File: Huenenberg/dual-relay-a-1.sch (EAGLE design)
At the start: 40 parts, among them J10 LARGE-SOLDERPAD, J11 LARGE-SOLDERPAD, J12 LARGE-SOLDERPAD, J13 LARGE-SOLDERPAD, J14 LARGE-SOLDERPAD, J15 LARGE-SOLDERPAD, J16 LARGE-SOLDERPAD, J17 LARGE-SOLDERPAD, J18 LARGE-SOLDERPAD, J19 LARGE-SOLDERPAD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

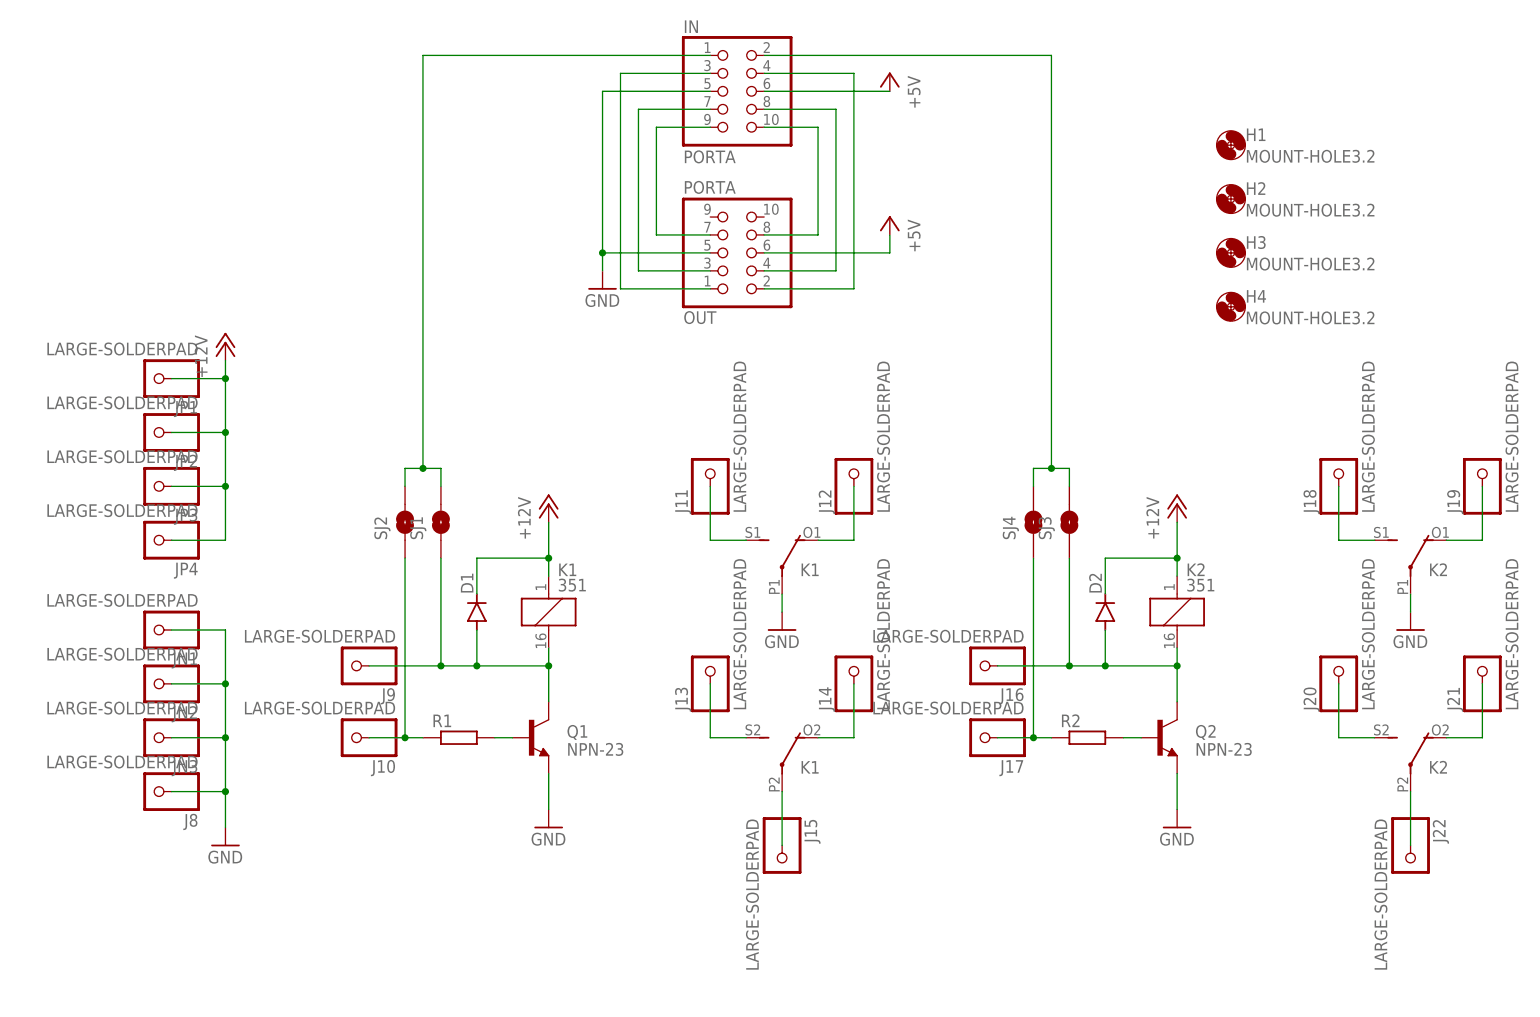
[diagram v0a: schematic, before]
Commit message: Adds values to the large solderpads that explain what should be connected.
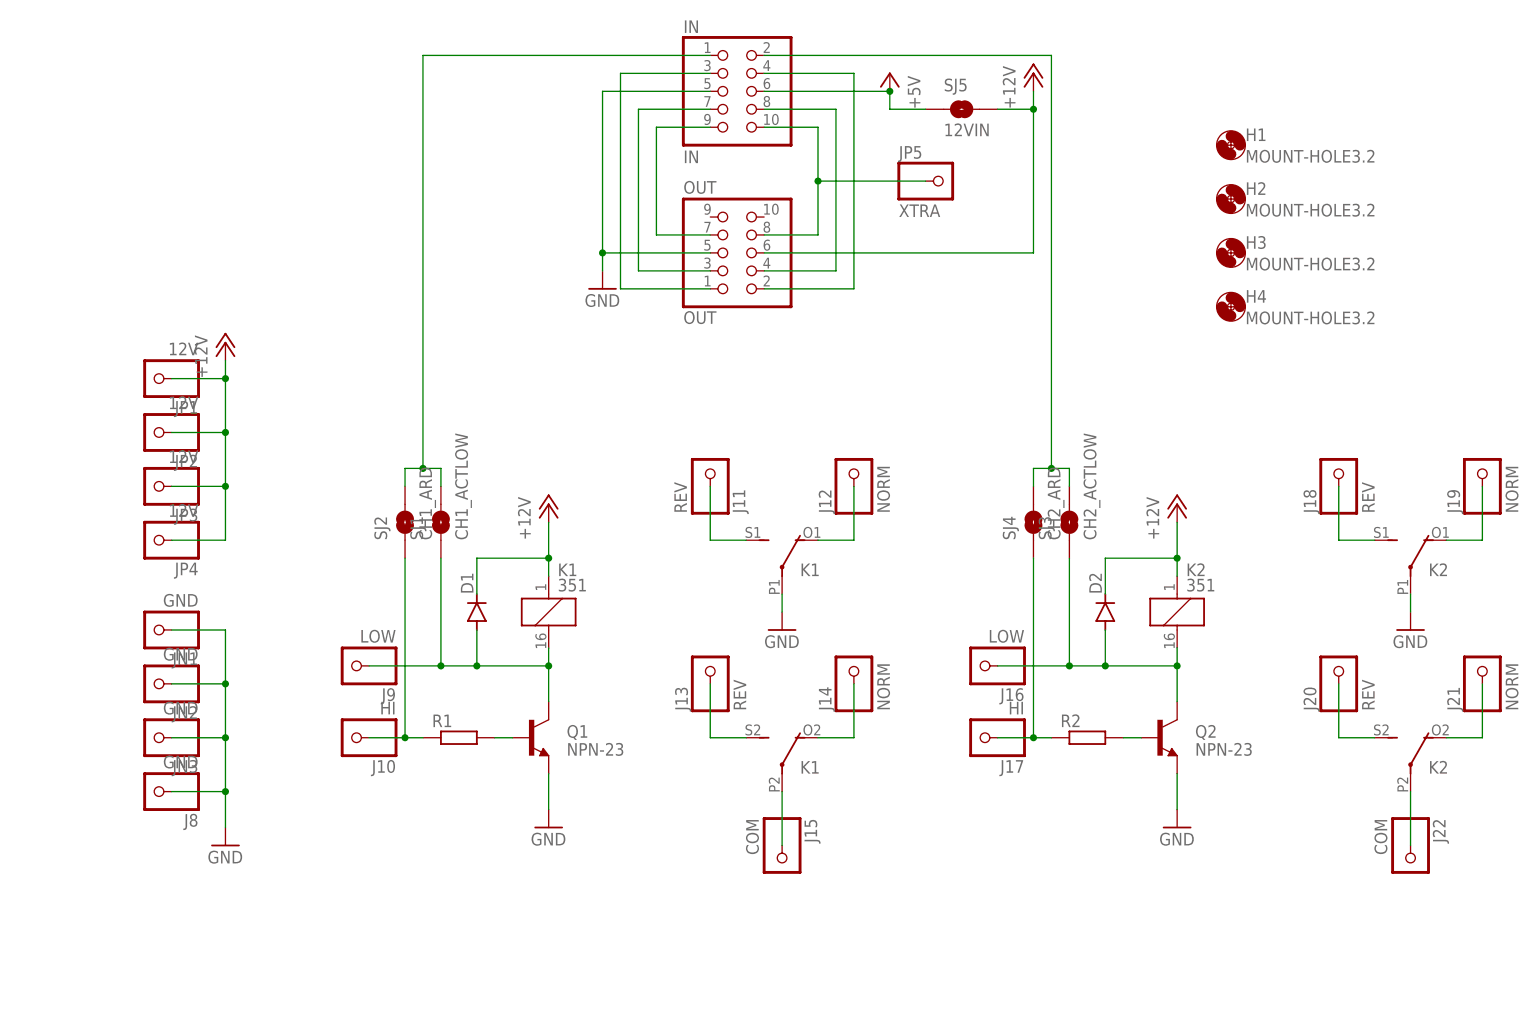
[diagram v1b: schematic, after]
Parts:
- added JP5: XTRA, eagleparts:LARGE-SOLDERPAD
- added SJ5: 12VIN, trainlib:SJRND2
- IN: value PORTA -> IN
- J10, J17: value LARGE-SOLDERPAD -> HI
- J11, J13, J18, J20: value LARGE-SOLDERPAD -> REV
- J12, J14, J19, J21: value LARGE-SOLDERPAD -> NORM
- J15, J22: value LARGE-SOLDERPAD -> COM
- J16, J9: value LARGE-SOLDERPAD -> LOW
- J8, JN1, JN2, JN3: value LARGE-SOLDERPAD -> GND
- JP1, JP2, JP3, JP4: value LARGE-SOLDERPAD -> 12V
- OUT: value PORTA -> OUT
- SJ1: value (none) -> CH1_ACTLOW
- SJ2: value (none) -> CH1_ARD
- SJ3: value (none) -> CH2_ACTLOW
- SJ4: value (none) -> CH2_ARD
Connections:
- net +12V: now also OUT.6, SJ5.2
- net +5V: now also SJ5.1; no longer OUT.6
- net N$22: now also JP5.1
